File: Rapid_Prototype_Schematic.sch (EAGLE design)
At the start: 37 parts, among them IC1 OP-AMP, IC2 OP-AMP, IC3 OP-AMP

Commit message: Added another sheet and created a amplifier schematic
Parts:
- added C22: (no value), adafruit:C-USC0805K
- added IC4: LM358D, linear:LM358D
- added R13, R14: (no value), adafruit:R-US_FLIPFLOP
- added U$1, U$2: (no value), adafruit:CR1220SMT
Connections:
- new net N$1: IC4A.+IN, R13.2
- new net N$11: IC4A.-IN, R13.1, U$2.-
- new net N$5: IC4A.OUT, R14.1
- new net N$7: C22.1, R14.2
- new net N$9: C22.2, U$1.-
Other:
- note added: "Alex's Test Schematic"

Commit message: started to work on esc module and added more sheets to schematic
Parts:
- removed U$1, U$2: (no value), adafruit:CR1220SMT
- added C23: 1, adafruit:C-USC0805
- added C24: 220, adafruit:C-US050-050X075
- C22: value (none) -> 0.1; device adafruit:C-USC0805K -> adafruit:C-USC0603
- IC4: value LM358D -> OP-AMP; device linear:LM358D -> SparkFun-IC-Amplifiers:OPAMP-DUALU
- R13: value (none) -> 0.005; device adafruit:R-US_FLIPFLOP -> adafruit:R-US_R1206
- R14: value (none) -> 3.3k; device adafruit:R-US_FLIPFLOP -> adafruit:R-US_R0603
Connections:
- removed net N$11: IC4A.-IN, R13.1, U$2.-
- removed net N$5: IC4A.OUT, R14.1
- removed net N$7: C22.1, R14.2
- removed net N$9: C22.2, U$1.-
- net 5V: now also C22.1
- net ESC_1_I: now also C23.1, R14.2
- net ESC_1_POWER: now also C24.1, IC4G1.-IN, R13.2
- net ESC_POWERS: now also IC4G1.+IN, R13.1
- net GND: now also C22.2, C23.2, C24.2
- net N$1: now also IC4G1.OUT, R14.1; no longer IC4A.+IN, R13.2
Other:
- note removed: "Alex's Test Schematic"

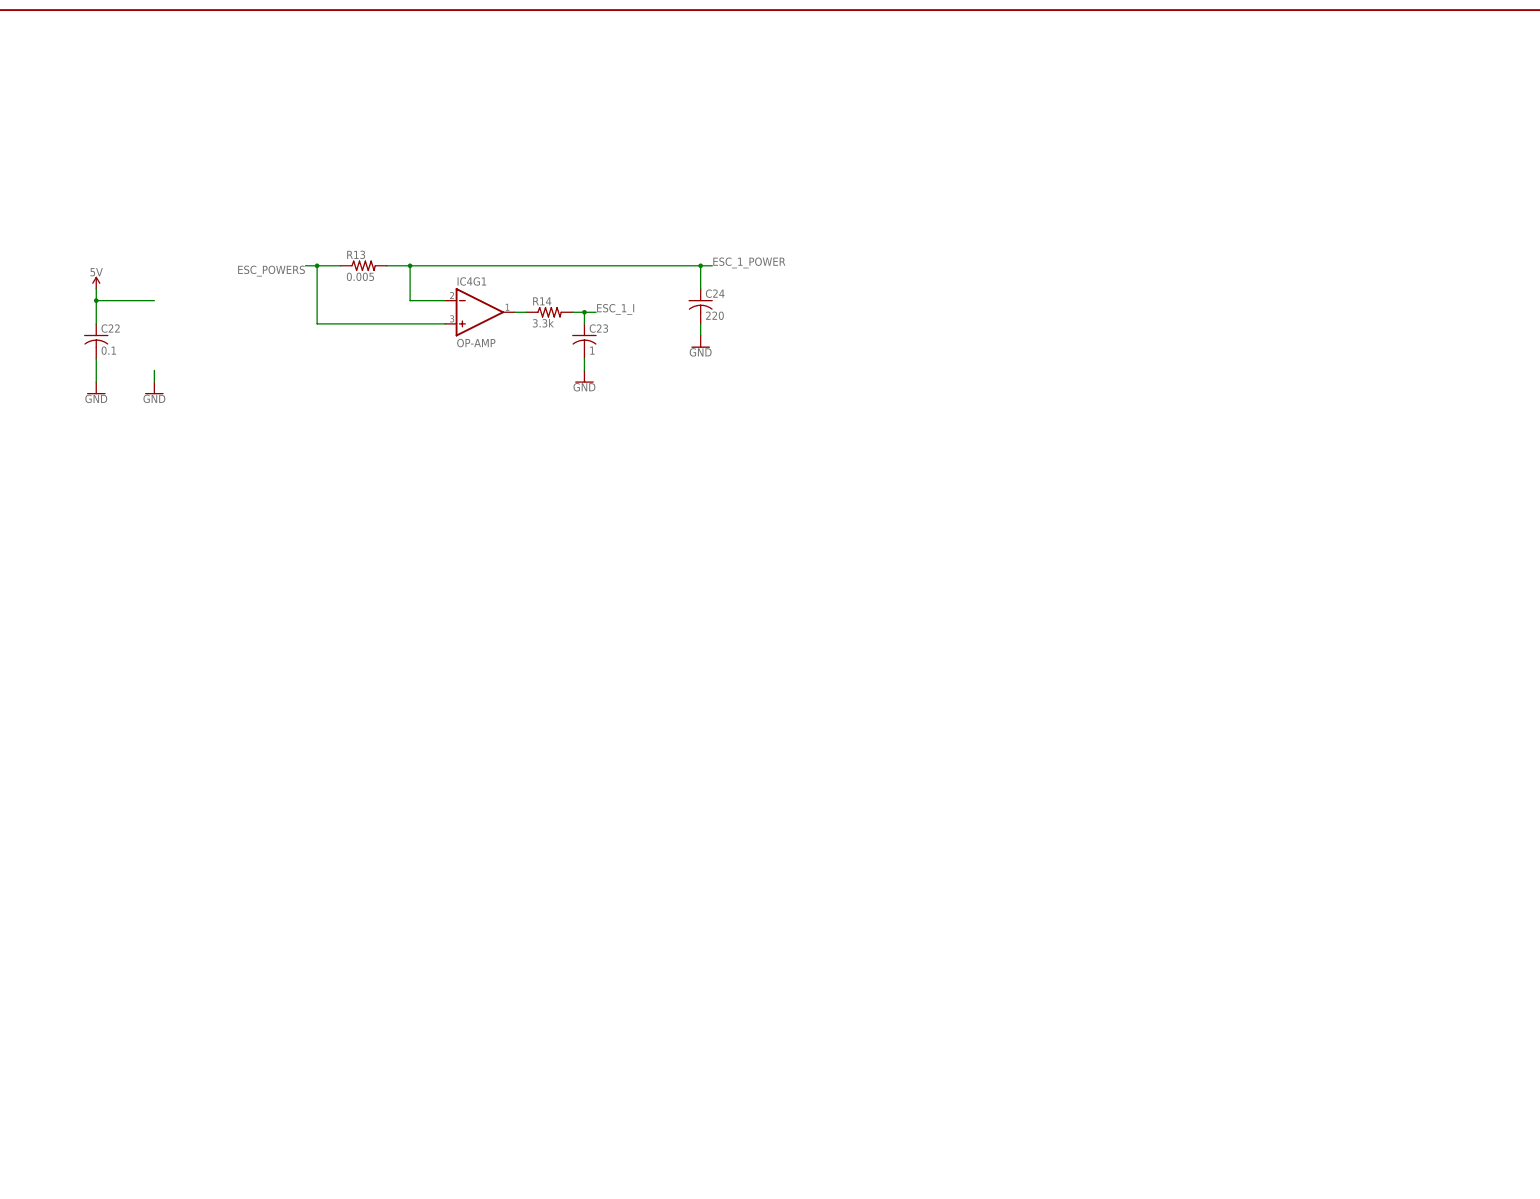
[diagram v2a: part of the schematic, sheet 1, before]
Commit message: Finished ESC circuit and started the Power Monitor Circuit
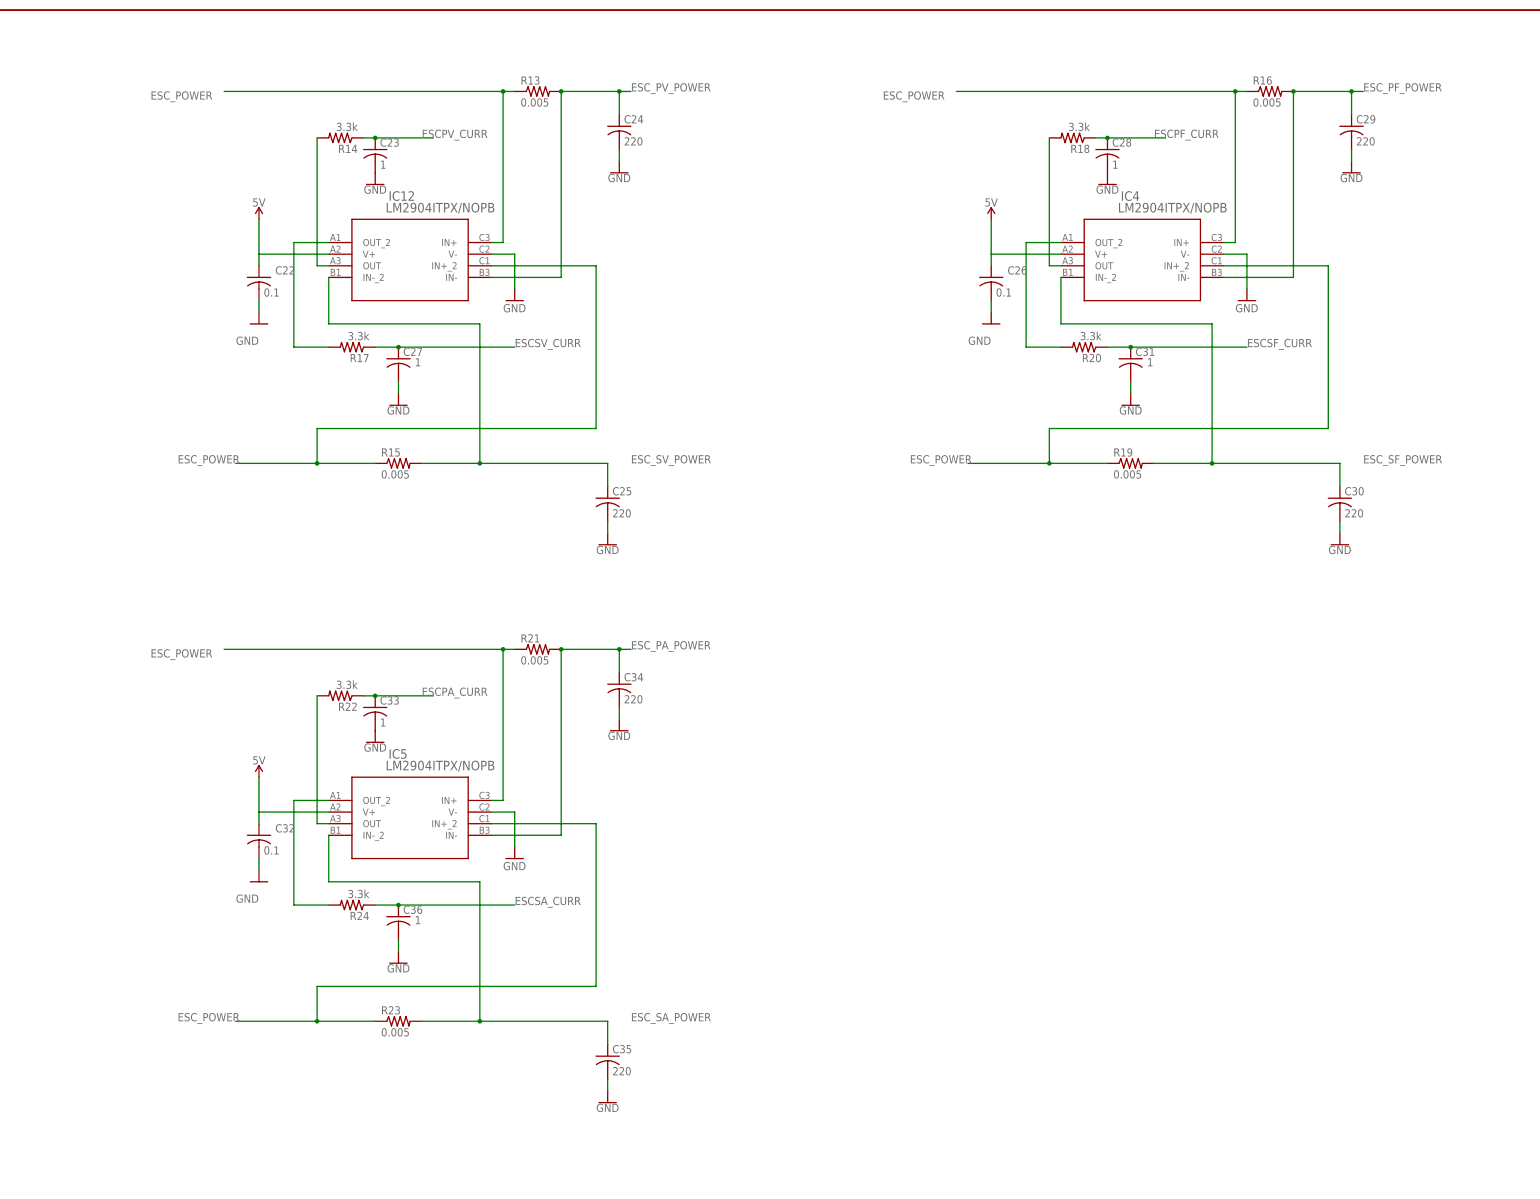
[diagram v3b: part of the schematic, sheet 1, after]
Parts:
- added C25, C29, C30, C34, C35: 220, adafruit:C-US050-050X075
- added C26, C32: 0.1, adafruit:C-USC0603
- added C27, C28, C31, C33, C36: 1, adafruit:C-USC0805
- added C37: (no value), adafruit:C-USC0805
- added CR1: BZT585B16T-7SOD523-M, Diode1:BZT585B16T-7SOD523-M
- added CR2: SMAJ18ASMASERIES-M, Diode2:SMAJ18ASMASERIES-M
- added IC12, IC5: LM2904ITPX/NOPB, Opamp1:LM2904ITPX/NOPB
- added R15, R16, R19, R21, R23: 0.005, adafruit:R-US_R1206
- added R17, R18, R20, R22, R24: 3.3k, adafruit:R-US_R0603
- added R25, R26, R27, R28: (no value), adafruit:R-US_R0603
- IC4: value OP-AMP -> LM2904ITPX/NOPB; device SparkFun-IC-Amplifiers:OPAMP-DUALU -> Opamp1:LM2904ITPX/NOPB
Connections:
- removed net ESC_POWERS: IC1G1.+IN, IC1G2.+IN, IC2G1.+IN, IC2G2.+IN, IC3G1.+IN, IC3G2.+IN, IC4G1.+IN, R1.1, R11.1, R13.1, R3.1, R5.1, R7.1, R9.1
- new net ESCPA_CURR: C33.1, R22.1
- new net ESCPF_CURR: C28.1, R18.1
- new net ESCPV_CURR: C23.1, R14.1
- new net ESCSA_CURR: C36.1, R24.1
- new net ESCSF_CURR: C31.1, R20.1
- new net ESCSV_CURR: C27.1, R17.1
- new net ESC_PA_POWER: C34.1, IC5.IN-, R21.2
- new net ESC_PF_POWER: C29.1, IC4.IN-, R16.2
- new net ESC_POWER: IC12.IN+, IC12.IN+_2, IC1G1.+IN, IC1G2.+IN, IC2G1.+IN, IC2G2.+IN, IC3G1.+IN, IC3G2.+IN, IC4.IN+, IC4.IN+_2, IC5.IN+, IC5.IN+_2, R1.1, R11.1, R13.1, R15.1, R16.1, R19.1, R21.1, R23.1, R3.1, R5.1, R7.1, R9.1
- new net ESC_PV_POWER: C24.1, IC12.IN-, R13.2
- new net ESC_SA_POWER: C35.1, IC5.IN-_2, R23.2
- new net ESC_SF_POWER: C30.1, IC4.IN-_2, R19.2
- new net ESC_SV_POWER: C25.1, IC12.IN-_2, R15.2
- new net N$11: IC5.OUT_2, R24.2
- new net N$13: C37.1, CR1.1, CR2.1, R25.2
- new net N$14: C37.2, CR1.2, CR2.2, R25.1
- new net N$2: IC4.OUT, R18.2
- new net N$5: IC12.OUT_2, R17.2
- new net N$7: IC4.OUT_2, R20.2
- new net N$9: IC5.OUT, R22.2
- net 5V: now also C26.1, C32.1, IC12.V+, IC4.V+, IC5.V+
- net ESC_1_I: no longer C23.1, R14.2
- net ESC_1_POWER: no longer C24.1, IC4G1.-IN, R13.2
- net GND: now also C25.2, C26.2, C27.2, C28.2, C29.2, C30.2, C31.2, C32.2, C33.2, C34.2, C35.2, C36.2, IC12.V-, IC4.V-, IC5.V-
- net N$1: now also IC12.OUT, R14.2; no longer IC4G1.OUT, R14.1
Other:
- moved on the sheet: C22, C23, C24, R13, R14

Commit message: Finished ESC Power circuit and started on Sensor Interface
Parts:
- removed CR1: BZT585B16T-7SOD523-M, Diode1:BZT585B16T-7SOD523-M
- removed CR2: SMAJ18ASMASERIES-M, Diode2:SMAJ18ASMASERIES-M
- added C38, C39, C40, C41, C42, C43: 1, adafruit:C-USC0805
- added D1, D3, D4, D5, D6, D7, D8: BZT585B16T-7SOD523-M, Diode1:BZT585B16T-7SOD523-M
- added D2: SMAJ18ASMASERIES-M, Diode2:SMAJ18ASMASERIES-M
- added R29, R32, R33, R36, R37, R40, R41, R44, R45, R48, R49, R52: 10k, adafruit:R-US_R0603
- added R30, R31, R34, R35, R38, R39, R42, R43, R46, R47, R50, R51: 1k, adafruit:R-US_R0603
- added R53: (no value), adafruit:R-US_R0603
- C37: value (none) -> 1
- R25, R28: value (none) -> 10k
- R26, R27: value (none) -> 1k
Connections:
- new net COMBINED_POWER: C37.1, D1.1, D2.1, R25.2
- new net ESCSA_SWITCH: R43.1
- new net ESCSFO_SWITCH: R39.1
- new net ESCSF_SWITCH: R51.1
- new net ESCSP_SWITCH: R47.1
- new net ESCSS_SWITCH: R31.1
- new net ESCSV_SWITCH: R35.1
- new net ESC_MAIN_POWER_SW: R27.1
- new net N$15: R26.1
- new net N$16: R31.2, R32.2
- new net N$17: R27.2, R28.2
- new net N$18: R30.1
- new net N$19: C39.2, D4.2, R33.1, R34.2
- new net N$20: R35.2, R36.2
- new net N$21: R34.1
- new net N$22: C40.2, D5.2, R37.1, R38.2
- new net N$23: R39.2, R40.2
- new net N$24: R38.1
- new net N$25: C41.2, D6.2, R41.1, R42.2
- new net N$26: R43.2, R44.2
- new net N$27: R42.1
- new net N$28: C42.2, D7.2, R45.1, R46.2
- new net N$29: R47.2, R48.2
- new net N$30: R46.1
- new net N$31: C43.2, D8.2, R49.1, R50.2
- new net N$32: R51.2, R52.2
- new net N$33: R50.1
- new net N$34: R53.1
- net ESC_POWER: now also C38.1, C39.1, C40.1, C41.1, C42.1, C43.1, D3.1, D4.1, D5.1, D6.1, D7.1, D8.1, R29.2, R33.2, R37.2, R41.2, R45.2, R49.2
- net GND: now also D2.2, R28.1, R32.1, R36.1, R40.1, R44.1, R48.1, R52.1, R53.2
- net N$13: now also C38.2, D3.2, R29.1, R30.2; no longer C37.1, CR1.1, CR2.1, R25.2
- net N$14: now also D1.2, R26.2; no longer CR1.2, CR2.2
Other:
- moved on the sheet: C37, Q1, Q2, R25, R26, R27, R28

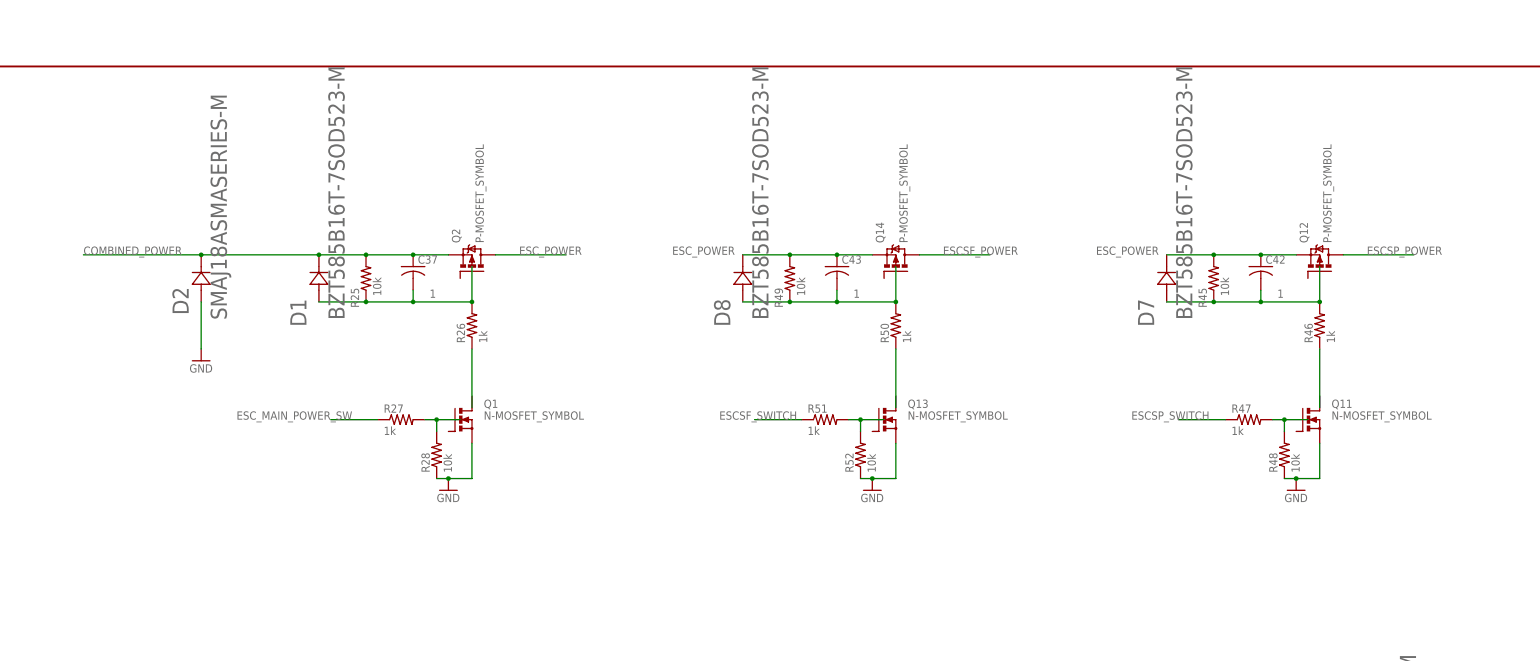
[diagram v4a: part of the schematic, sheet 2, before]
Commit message: Finished updated Sensor interface started work on Battery  Voltage Circuit.
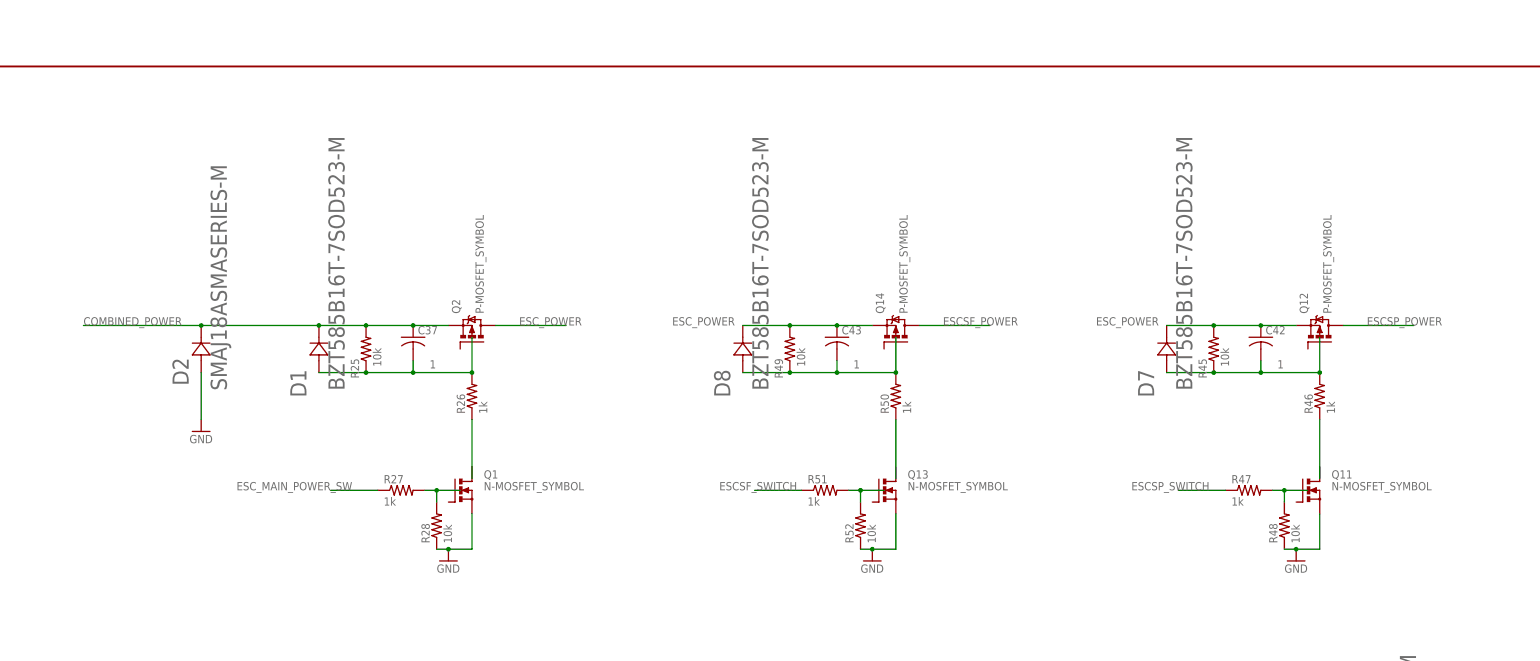
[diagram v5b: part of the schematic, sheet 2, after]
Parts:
- added C44, C45: 1, adafruit:C-USC0603
- added D10, D9: MBD701, diode:MBD701
- added IC6, IC7: OP-AMP, SparkFun-IC-Amplifiers:OPAMP-DUALU
- added R54, R55: 5M, adafruit:R-US_R0603
- added R56, R57, R58: (no value), adafruit:R-US_M0805
- R53: value (none) -> 1M
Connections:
- net N$34 renamed J1
- new net BATTERY_1+: C44.1, D9.A
- new net BATTERY_2+: C45.1, D10.A
- new net LK_DET_MAIN: R56.1
- new net LK_DET_P_BAT: R57.1
- new net LK_DET_S_BAT: R58.1
- new net PORT_BAT_CURR: D9.C, IC6G3.P$V+, R54.1
- new net STBD_BAT_CURR: D10.C, IC7G3.P$V+, R55.1
- net 5V: now also R53.2, R56.2, R57.2, R58.2
- net COMBINED_POWER: now also IC6G3.P$V-, IC7G3.P$V-, R54.2, R55.2
- net GND: now also C44.2, C45.2; no longer R53.2
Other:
- moved on the sheet: C37, C42, C43, D1, D2, D7, D8, Q1, Q11, Q12, Q13, Q14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
